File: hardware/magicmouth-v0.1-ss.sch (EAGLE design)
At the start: 27 parts, among them IC1 LM386N, IC2 ATMEGA168-20P, J1 1X2-3.5MM, Q1 16Mhz, U1 ARDUINOR3-NOIOREF-NOTEXT, X1 STEREOJACK

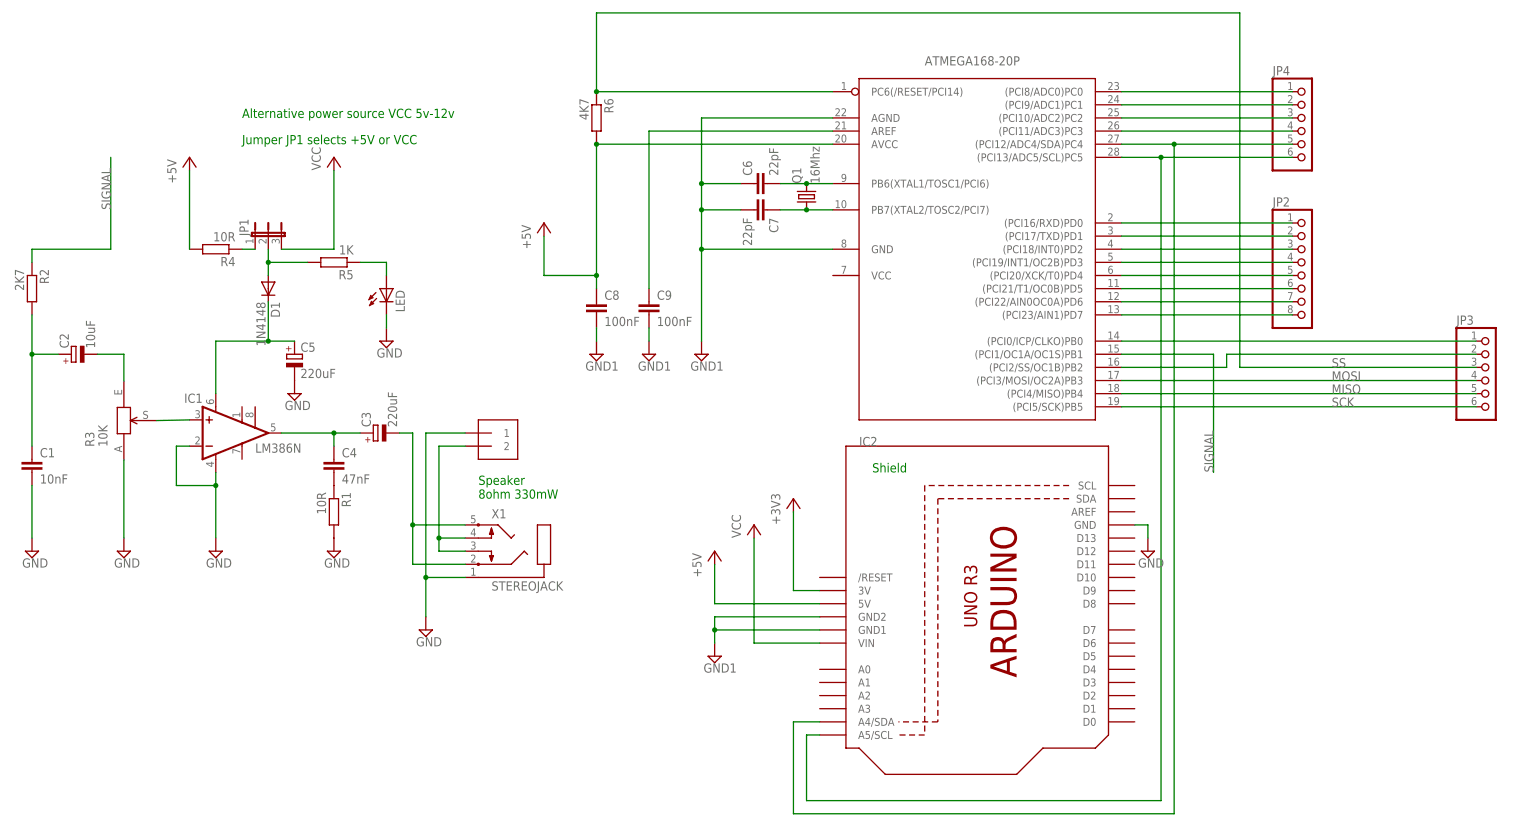
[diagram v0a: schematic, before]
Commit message: added programming jumpers
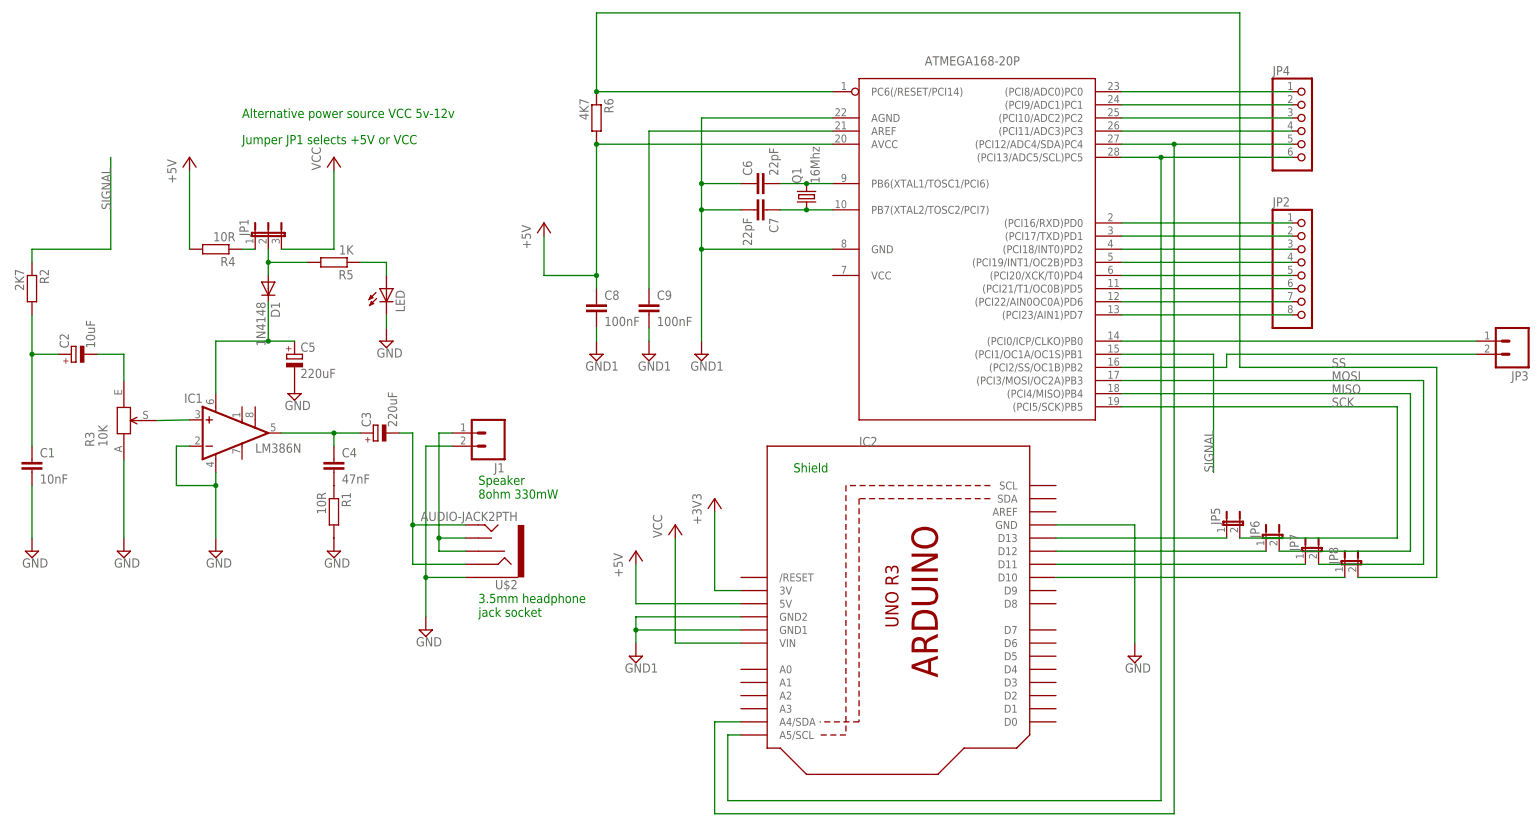
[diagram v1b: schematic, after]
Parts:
- removed X1: STEREOJACK, adafruit:STEREOJACK
- added JP5, JP6, JP7, JP8: (no value), SparkFun-Passives:JUMPER-2PTH
- added U$2: AUDIO-JACK2PTH, SparkFun-Connectors:AUDIO-JACK2PTH
- C1: device resistor:C-EU025-025X050 -> resistor:C-EU050-025X075
- C4, C8, C9: device rcl:C-EU025-025X050 -> resistor:C-EU050-025X075
- J1: value 1X2-3.5MM -> (none); device adafruit:1X2-3.5MM -> SparkFun-Connectors:M023.5MM
- JP3: device adafruit:PINHD-1X6B -> SparkFun-Connectors:M021X02_NO_SILK
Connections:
- new net N$25: JP5.1, U1.D13
- new net N$26: JP6.1, U1.D12
- new net N$28: JP7.1, U1.D11
- new net N$29: JP8.1, U1.D10
- net GND: now also J1.2, U$2.SLEEVE; no longer J1.1, X1.1
- net MISO: now also JP6.2; no longer JP3.5
- net MOSI: now also JP7.2; no longer JP3.4
- net N$3: now also J1.1, U$2.RSH, U$2.TSH; no longer J1.2, X1.3, X1.4
- net N$8: now also U$2.RING, U$2.TIP; no longer X1.2, X1.5
- net SCK: now also JP5.2; no longer JP3.6
- net SS: now also JP8.2; no longer JP3.3
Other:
- note added: "3.5mm headphone jack socket"

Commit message: reset switch on ss board; optional capacitor
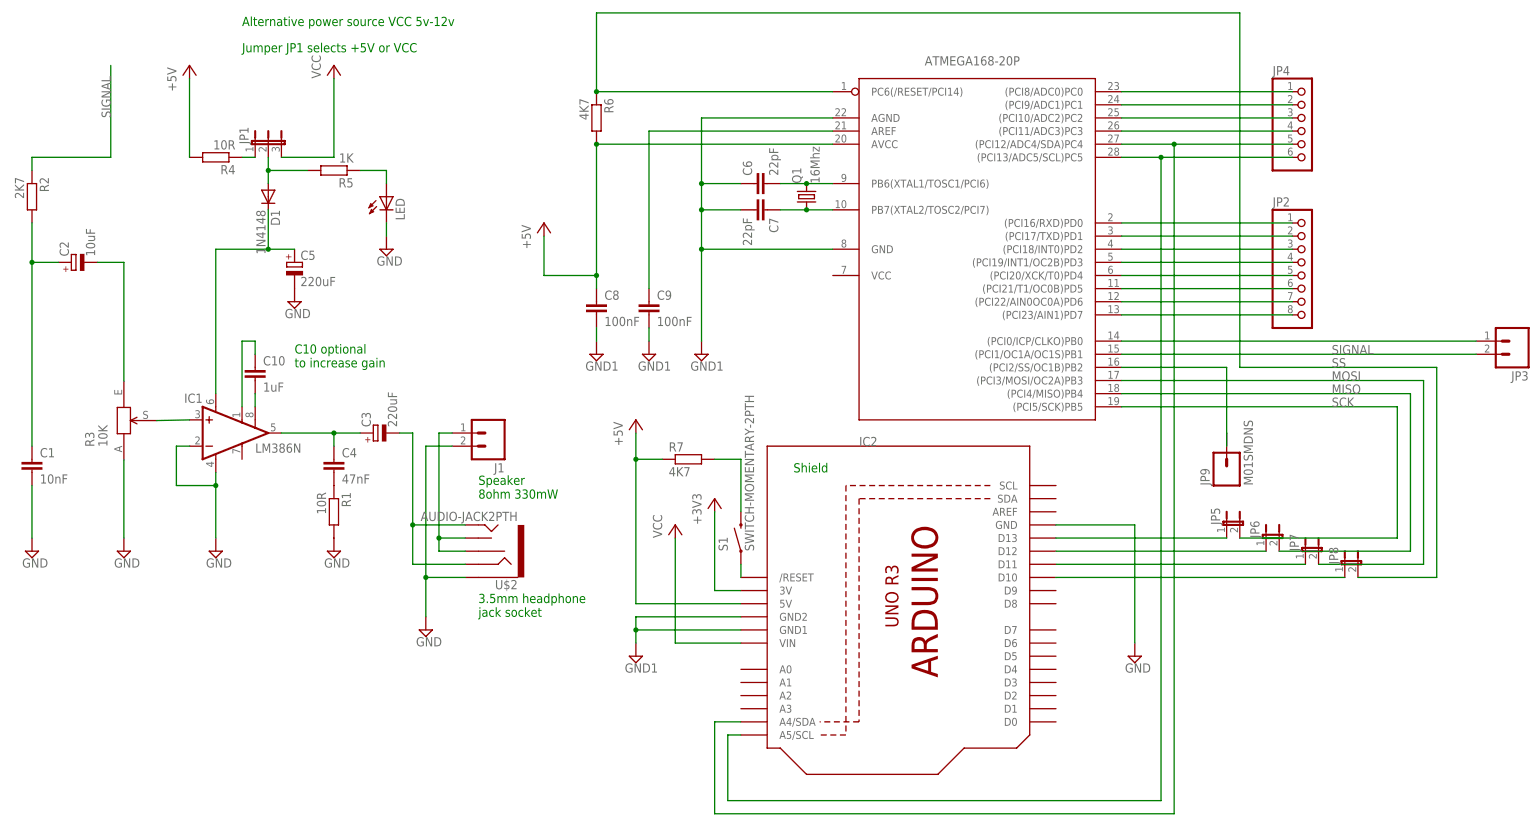
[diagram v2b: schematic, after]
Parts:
- added C10: 1uF, resistor:C-EU050-025X075
- added JP9: M01SMDNS, SparkFun-Connectors:M01SMDNS
- added R7: 4K7, rcl:R-EU_0207/7
- added S1: SWITCH-MOMENTARY-2PTH, SparkFun-Electromechanical:SWITCH-MOMENTARY-2PTH
- C2: device resistor:CPOL-EUE2.5-6 -> rcl:CPOL-EUE2.5-7
- C8, C9: device resistor:C-EU050-025X075 -> rcl:C-EU025-025X050
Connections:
- new net N$34: R7.2, S1.2
- new net N$35: S1.1, U1./RESET
- new net N$36: C10.2, IC1.GAIN@2
- new net N$37: C10.1, IC1.GAIN@1
- net +5V: now also R7.1
- net N$12: now also JP9.1; no longer JP3.2
- net SIGNAL: now also JP3.2
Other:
- note added: "C10 optional to increase gain"
- moved on the sheet: C2, C5, D1, JP1, LED, R2, R4, R5

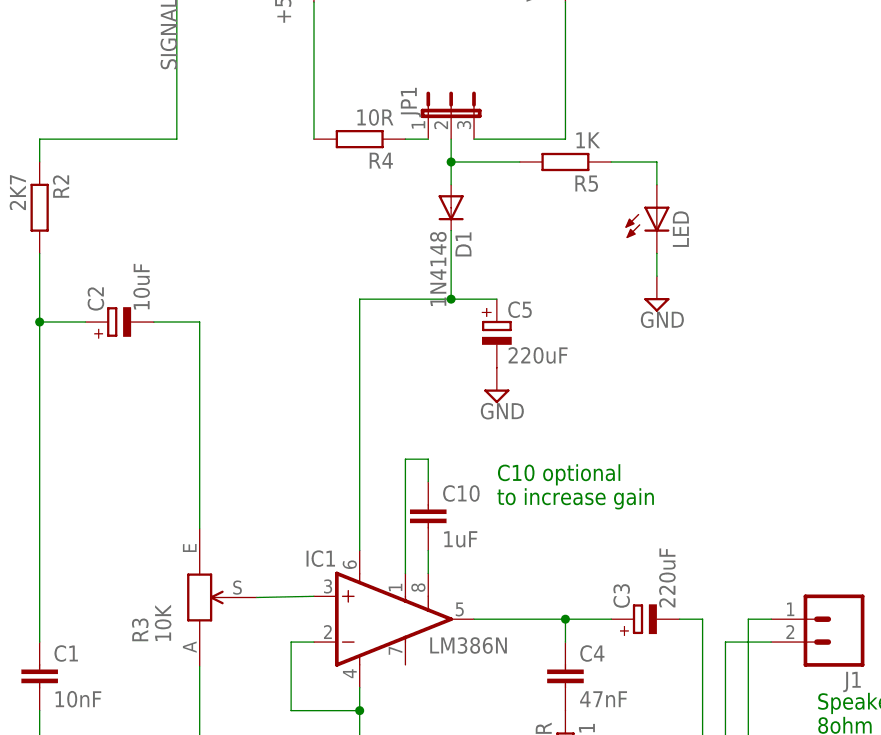
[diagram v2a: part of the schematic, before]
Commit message: 220K resistor in series with gain control
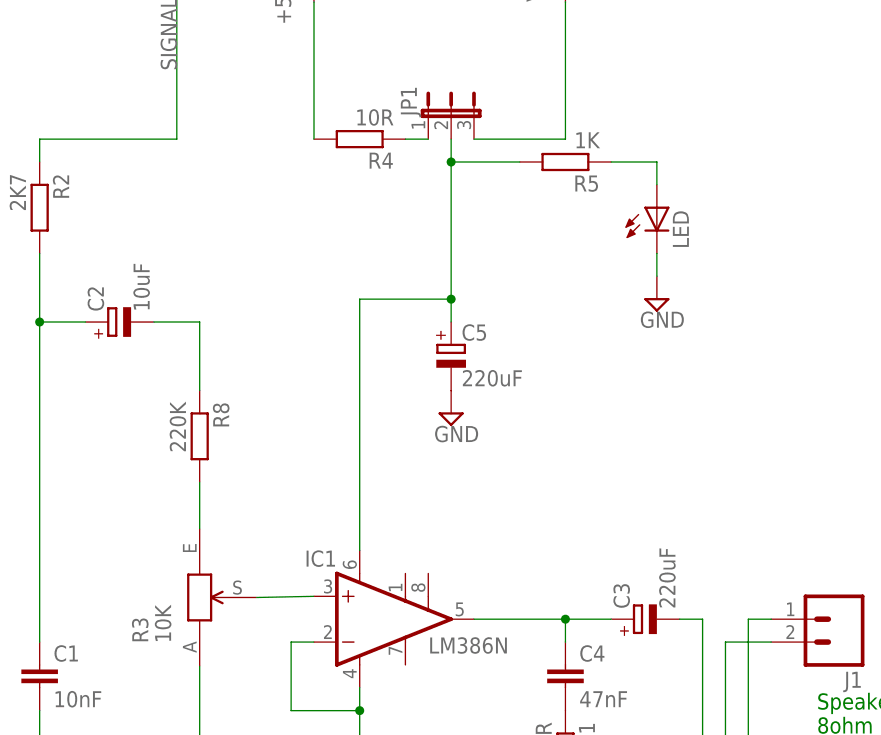
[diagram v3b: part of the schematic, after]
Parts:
- removed C10: 1uF, resistor:C-EU050-025X075
- removed D1: 1N4148, diode:1N4148DO35-7
- added R8: 220K, rcl:R-EU_0207/7
- JP2: device adafruit:PINHD-1X8BIG -> adafruit:PINHD-1X8CLEANBIG
- JP4: device adafruit:PINHD-1X6B -> adafruit:PINHD-1X6CB
- R2: device resistor:R-EU_0207/10 -> rcl:R-EU_0207/7
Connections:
- removed net N$27: D1.A, JP1.2, R5.2
- removed net N$37: C10.1, IC1.GAIN@1
- net N$36: now also R3.E, R8.2; no longer C10.2, IC1.GAIN@2
- net N$5: now also R8.1; no longer R3.E
- net VS: now also JP1.2, R5.2; no longer D1.C
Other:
- note removed: "C10 optional to increase gain"
- moved on the sheet: C5
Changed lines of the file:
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@@
 <part name="IC1" library="linear" deviceset="LM386?-*" device="N" technology="1" value="LM386N"/>
 <part name="R1" library="resistor" deviceset="R-EU_" device="0207/7" value="10R"/>
-<part name="R2" library="resistor" deviceset="R-EU_" device="0207/10" value="2K7"/>
+<part name="R2" library="rcl" deviceset="R-EU_" device="0207/7" value="2K7"/>
 <part name="GND1" library="supply2" deviceset="GND" device=""/>
 <part name="C1" library="resistor" deviceset="C-EU" device="050-025X075" value="10nF"/>
@@
 <part name="GND3" library="supply2" deviceset="GND" device=""/>
 <part name="JP1" library="jumper" deviceset="JP2E" device=""/>
-<part name="D1" library="diode" deviceset="1N4148" device="DO35-7" value="1N4148"/>
 <part name="R5" library="rcl" deviceset="R-EU_" device="0207/7" value="1K"/>
 <part name="LED" library="led" deviceset="LED" device="3MM"/>
@@
 <part name="GND12" library="supply2" deviceset="GND1" device=""/>
 <part name="GND13" library="supply2" deviceset="GND1" device=""/>
-<part name="JP2" library="adafruit" deviceset="PINHD-1X8" device="BIG"/>
+<part name="JP2" library="adafruit" deviceset="PINHD-1X8" device="CLEANBIG"/>
 <part name="P+1" library="supply1" deviceset="VCC" device=""/>
 <part name="P+2" library="supply1" deviceset="VCC" device=""/>
 <part name="GND14" library="supply2" deviceset="GND" device=""/>
-<part name="JP4" library="adafruit" deviceset="PINHD-1X6" device="B"/>
+<part name="JP4" library="adafruit" deviceset="PINHD-1X6" device="CB"/>
 <part name="J1" library="SparkFun-Connectors" deviceset="M02" device="3.5MM"/>
 <part name="P+5" library="supply1" deviceset="+5V" device=""/>
@@
 <attribute name="RESISTANCE" value="4K7"/>
 </part>
-<part name="C10" library="resistor" deviceset="C-EU" device="050-025X075" value="1uF"/>
 <part name="JP9" library="SparkFun-Connectors" deviceset="M01" device="SMDNS" value="M01SMDNS"/>
+<part name="R8" library="rcl" deviceset="R-EU_" device="0207/7" value="220K"/>
 </parts>
 <sheets>
@@
 <text x="109.22" y="27.94" size="1.778" layer="91">3.5mm headphone
 jack socket</text>
-<text x="73.66" y="76.2" size="1.778" layer="91">C10 optional
-to increase gain</text>
 </plain>
 <instances>
@@
 <instance part="GND6" gate="GND" x="99.06" y="25.4"/>
 <instance part="R4" gate="G$1" x="58.42" y="116.84" rot="R180"/>
-<instance part="C5" gate="G$1" x="73.66" y="96.52"/>
-<instance part="GND3" gate="GND" x="73.66" y="88.9"/>
+<instance part="C5" gate="G$1" x="68.58" y="93.98"/>
+<instance part="GND3" gate="GND" x="68.58" y="86.36"/>
 <instance part="JP1" gate="1" x="68.58" y="119.38"/>
-<instance part="D1" gate="G$1" x="68.58" y="109.22" rot="R270"/>
 <instance part="R5" gate="G$1" x="81.28" y="114.3" rot="R180"/>
 <instance part="LED" gate="G$1" x="91.44" y="109.22"/>
@@
 <instance part="S1" gate="G$1" x="160.02" y="43.18" rot="R90"/>
 <instance part="R7" gate="G$1" x="149.86" y="58.42"/>
-<instance part="C10" gate="G$1" x="66.04" y="76.2"/>
 <instance part="JP9" gate="G$1" x="254" y="55.88" rot="R90"/>
+<instance part="R8" gate="G$1" x="40.64" y="83.82" rot="R270"/>
 </instances>
 <busses>
@@
 <wire x1="35.56" y1="96.52" x2="40.64" y2="96.52" width="0.1524" layer="91"/>
 <pinref part="C2" gate="G$1" pin="-"/>
-<pinref part="R3" gate="G$1" pin="E"/>
-<wire x1="40.64" y1="73.533" x2="40.64" y2="96.52" width="0.1524" layer="91"/>
+<pinref part="R8" gate="G$1" pin="1"/>
+<wire x1="40.64" y1="88.9" x2="40.64" y2="96.52" width="0.1524" layer="91"/>
 </segment>
 </net>
@@
 <segment>
 <wire x1="58.42" y1="71.12" x2="58.42" y2="99.06" width="0.1524" layer="91"/>
-<wire x1="73.66" y1="99.06" x2="68.58" y2="99.06" width="0.1524" layer="91"/>
+<wire x1="68.58" y1="96.52" x2="68.58" y2="99.06" width="0.1524" layer="91"/>
 <wire x1="68.58" y1="99.06" x2="58.42" y2="99.06" width="0.1524" layer="91"/>
-<wire x1="68.58" y1="106.68" x2="68.58" y2="99.06" width="0.1524" layer="91"/>
+<wire x1="68.58" y1="114.3" x2="68.58" y2="99.06" width="0.1524" layer="91"/>
 <junction x="68.58" y="99.06"/>
 <pinref part="IC1" gate="G$1" pin="VS"/>
 <pinref part="C5" gate="G$1" pin="+"/>
-<pinref part="D1" gate="G$1" pin="C"/>
+<pinref part="JP1" gate="1" pin="2"/>
+<pinref part="R5" gate="G$1" pin="2"/>
+<wire x1="68.58" y1="114.3" x2="68.58" y2="116.84" width="0.1524" layer="91"/>
+<wire x1="76.2" y1="114.3" x2="68.58" y2="114.3" width="0.1524" layer="91"/>
+<junction x="68.58" y="114.3"/>
 </segment>
 </net>
@@
 </segment>
 </net>
-<net name="N$27" class="0">
-<segment>
-<wire x1="68.58" y1="111.76" x2="68.58" y2="114.3" width="0.1524" layer="91"/>
-<pinref part="JP1" gate="1" pin="2"/>
-<pinref part="D1" gate="G$1" pin="A"/>
-<pinref part="R5" gate="G$1" pin="2"/>
-<wire x1="68.58" y1="114.3" x2="68.58" y2="116.84" width="0.1524" layer="91"/>
-<wire x1="76.2" y1="114.3" x2="68.58" y2="114.3" width="0.1524" layer="91"/>
-<junction x="68.58" y="114.3"/>
-</segment>
-</net>
 <net name="+3V3" class="0">
 <segment>
@@
 </segment>
 </net>
-<net name="N$36" class="0">
-<segment>
-<pinref part="IC1" gate="G$1" pin="GAIN@2"/>
-<pinref part="C10" gate="G$1" pin="2"/>
-<wire x1="66.04" y1="68.58" x2="66.04" y2="71.12" width="0.1524" layer="91"/>
-</segment>
-</net>
-<net name="N$37" class="0">
-<segment>
-<pinref part="C10" gate="G$1" pin="1"/>
-<wire x1="66.04" y1="78.74" x2="66.04" y2="81.28" width="0.1524" layer="91"/>
-<wire x1="66.04" y1="81.28" x2="63.5" y2="81.28" width="0.1524" layer="91"/>
-<pinref part="IC1" gate="G$1" pin="GAIN@1"/>
-<wire x1="63.5" y1="81.28" x2="63.5" y2="68.58" width="0.1524" layer="91"/>
-</segment>
-</net>
 <net name="N$12" class="0">
 <segment>
@@
 </segment>
 </net>
+<net name="N$36" class="0">
+<segment>
+<pinref part="R3" gate="G$1" pin="E"/>
+<pinref part="R8" gate="G$1" pin="2"/>
+<wire x1="40.64" y1="73.533" x2="40.64" y2="78.74" width="0.1524" layer="91"/>
+</segment>
+</net>
